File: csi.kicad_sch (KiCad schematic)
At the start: 69 parts, among them J10 Conn_01x22_MountingPin, J11 Conn_01x22_MountingPin, J8 Conn_01x22_MountingPin, J9 Conn_01x22_MountingPin, U16 PI4MSD5V9548AZDEX, U17 AP22615A, U18 AP22615A, U19 AP22615A, U20 AP22615A, U21 NTS0102, U22 NTS0102

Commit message: DRC cleanup
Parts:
- U16: footprint JetsonCarrier:VQFN-24-1EP_3.8x3.8x1.0mm_P0.5mm -> Argus-IC:TQFN-24-1EP_4x4mm_P0.5mm_EP2.3x2.3mm
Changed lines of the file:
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@@
 			)
 		)
-		(property "Footprint" "JetsonCarrier:VQFN-24-1EP_3.8x3.8x1.0mm_P0.5mm"
+		(property "Footprint" "Argus-IC:TQFN-24-1EP_4x4mm_P0.5mm_EP2.3x2.3mm"
 			(at 106.68 66.04 0)
 			(hide yes)

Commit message: Move parts under SoM to bottom for thinner module connector
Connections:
- net VSYNC_CAM0: now also U21.5 (A_{1}); no longer U21.4 (A_{2})
- net VSYNC_CAM0_3V3: now also U21.8 (B_{1}); no longer U21.1 (B_{2})
- net VSYNC_CAM1: now also U21.4 (A_{2}); no longer U21.5 (A_{1})
- net VSYNC_CAM1_3V3: now also U21.1 (B_{2}); no longer U21.8 (B_{1})
- net VSYNC_CAM2: now also U22.5 (A_{1}); no longer U22.4 (A_{2})
- net VSYNC_CAM2_3V3: now also U22.8 (B_{1}); no longer U22.1 (B_{2})
- net VSYNC_CAM3: now also U22.4 (A_{2}); no longer U22.5 (A_{1})
- net VSYNC_CAM3_3V3: now also U22.1 (B_{2}); no longer U22.8 (B_{1})
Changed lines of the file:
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@@
 	)
 	(label "VSYNC_CAM0_3V3"
-		(at 382.27 198.12 180)
+		(at 382.27 195.58 180)
 		(effects
 			(font
@@
 	)
 	(label "VSYNC_CAM1_3V3"
-		(at 382.27 195.58 180)
+		(at 382.27 198.12 180)
 		(effects
 			(font
@@
 	)
 	(label "VSYNC_CAM3_3V3"
-		(at 382.27 227.33 180)
+		(at 382.27 229.87 180)
 		(effects
 			(font
@@
 	)
 	(label "VSYNC_CAM2_3V3"
-		(at 382.27 229.87 180)
+		(at 382.27 227.33 180)
 		(effects
 			(font
@@
 	(global_label "VSYNC_CAM0"
 		(shape input)
-		(at 341.63 198.12 180)
-		(fields_autoplaced yes)
-		(effects
-			(font
-				(size 1.27 1.27)
-			)
-			(justify right)
-		)
-		(property "Intersheetrefs" "${INTERSHEET_REFS}"
-			(at 327.2426 198.1994 0)
+		(at 341.63 195.58 180)
+		(fields_autoplaced yes)
+		(effects
+			(font
+				(size 1.27 1.27)
+			)
+			(justify right)
+		)
+		(property "Intersheetrefs" "${INTERSHEET_REFS}"
+			(at 327.2426 195.5006 0)
 			(show_name no)
 			(do_not_autoplace no)
@@
 	(global_label "VSYNC_CAM2"
 		(shape input)
+		(at 341.63 227.33 180)
+		(fields_autoplaced yes)
+		(effects
+			(font
+				(size 1.27 1.27)
+			)
+			(justify right)
+		)
+		(property "Intersheetrefs" "${INTERSHEET_REFS}"
+			(at 327.2426 227.2506 0)
+			(show_name no)
+			(do_not_autoplace no)
+			(effects
+				(font
+					(size 1.27 1.27)
+				)
+				(justify right)
+			)
+		)
+	)
+	(global_label "CSI2_CLK_P"
+		(shape input)
+		(at 295.91 95.25 180)
+		(fields_autoplaced yes)
+		(effects
+			(font
+				(size 1.27 1.27)
+			)
+			(justify right)
+		)
+		(property "Intersheetrefs" "${INTERSHEET_REFS}"
+			(at 282.4298 95.3294 0)
+			(show_name no)
+			(do_not_autoplace no)
+			(effects
+				(font
+					(size 1.27 1.27)
+				)
+				(justify right)
+			)
+		)
+	)
+	(global_label "VSYNC_CAM3"
+		(shape input)
 		(at 341.63 229.87 180)
 		(fields_autoplaced yes)
@@
 		)
 		(property "Intersheetrefs" "${INTERSHEET_REFS}"
-			(at 327.2426 229.9494 0)
-			(show_name no)
-			(do_not_autoplace no)
-			(effects
-				(font
-					(size 1.27 1.27)
-				)
-				(justify right)
-			)
-		)
-	)
-	(global_label "CSI2_CLK_P"
-		(shape input)
-		(at 295.91 95.25 180)
-		(fields_autoplaced yes)
-		(effects
-			(font
-				(size 1.27 1.27)
-			)
-			(justify right)
-		)
-		(property "Intersheetrefs" "${INTERSHEET_REFS}"
-			(at 282.4298 95.3294 0)
-			(show_name no)
-			(do_not_autoplace no)
-			(effects
-				(font
-					(size 1.27 1.27)
-				)
-				(justify right)
-			)
-		)
-	)
-	(global_label "VSYNC_CAM3"
-		(shape input)
-		(at 341.63 227.33 180)
-		(fields_autoplaced yes)
-		(effects
-			(font
-				(size 1.27 1.27)
-			)
-			(justify right)
-		)
-		(property "Intersheetrefs" "${INTERSHEET_REFS}"
-			(at 327.2426 227.4094 0)
+			(at 327.2426 229.7906 0)
 			(show_name no)
 			(do_not_autoplace no)
@@
 	(global_label "VSYNC_CAM1"
 		(shape input)
-		(at 341.63 195.58 180)
-		(fields_autoplaced yes)
-		(effects
-			(font
-				(size 1.27 1.27)
-			)
-			(justify right)
-		)
-		(property "Intersheetrefs" "${INTERSHEET_REFS}"
-			(at 327.2426 195.6594 0)
-			(show_name no)
-			(do_not_autoplace no)
+		(at 341.63 198.12 180)
+		(fields_autoplaced yes)
+		(effects
+			(font
+				(size 1.27 1.27)
+			)
+			(justify right)
+		)
+		(property "Intersheetrefs" "${INTERSHEET_REFS}"
+			(at 327.2426 198.0406 0)
+			(show_name no)
+			(do_not_autoplace no)

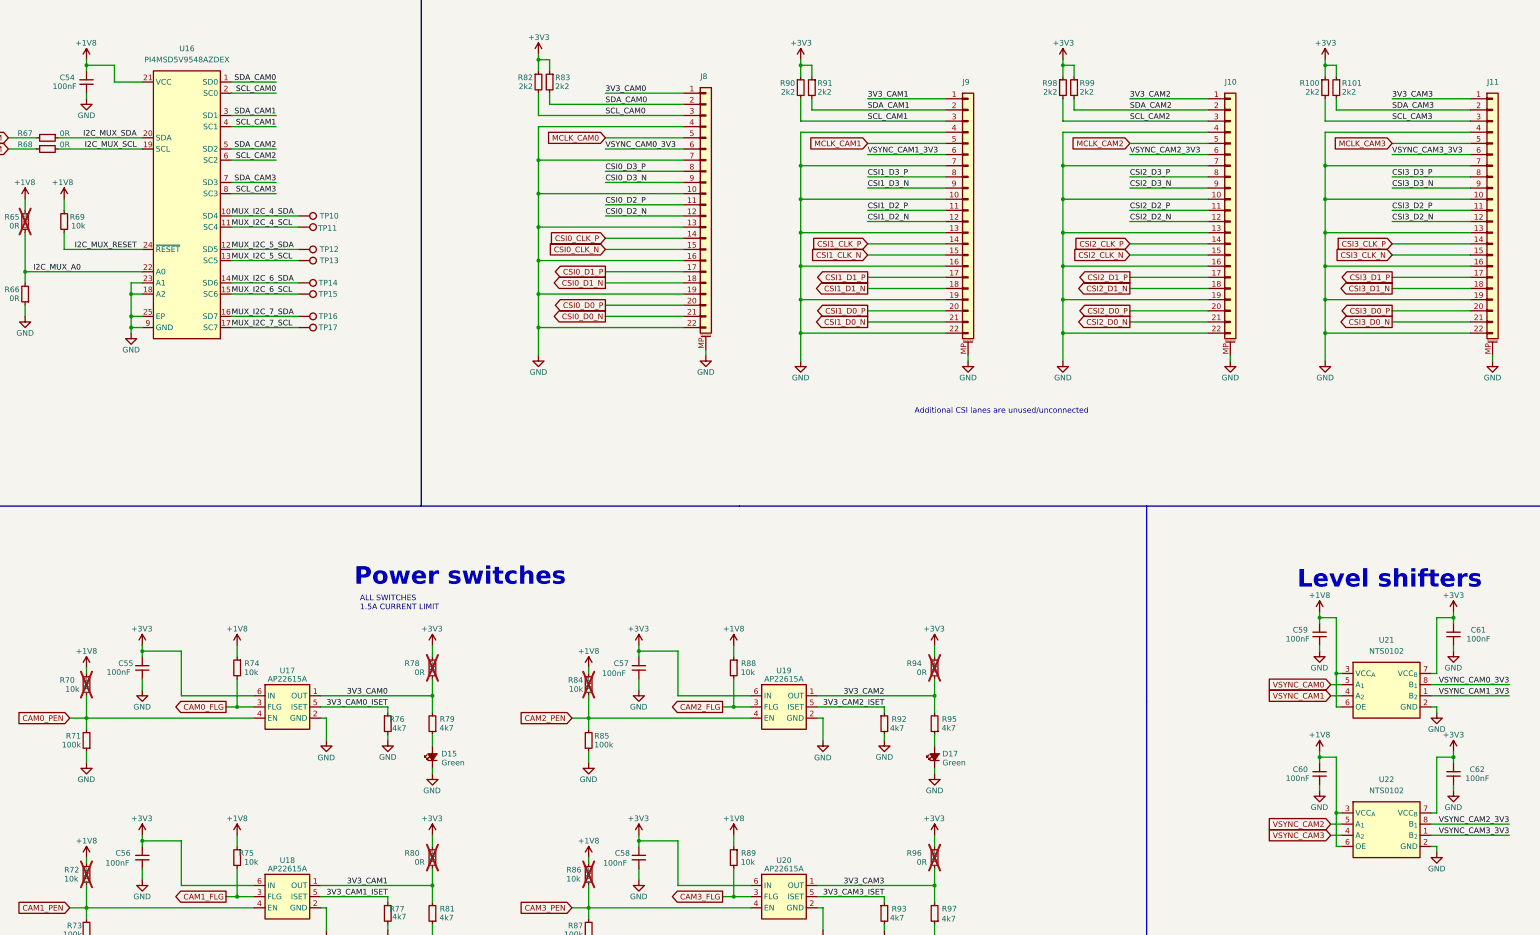
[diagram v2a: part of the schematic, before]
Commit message: Replace current monitor w/ INA226 (addr = 0x42)
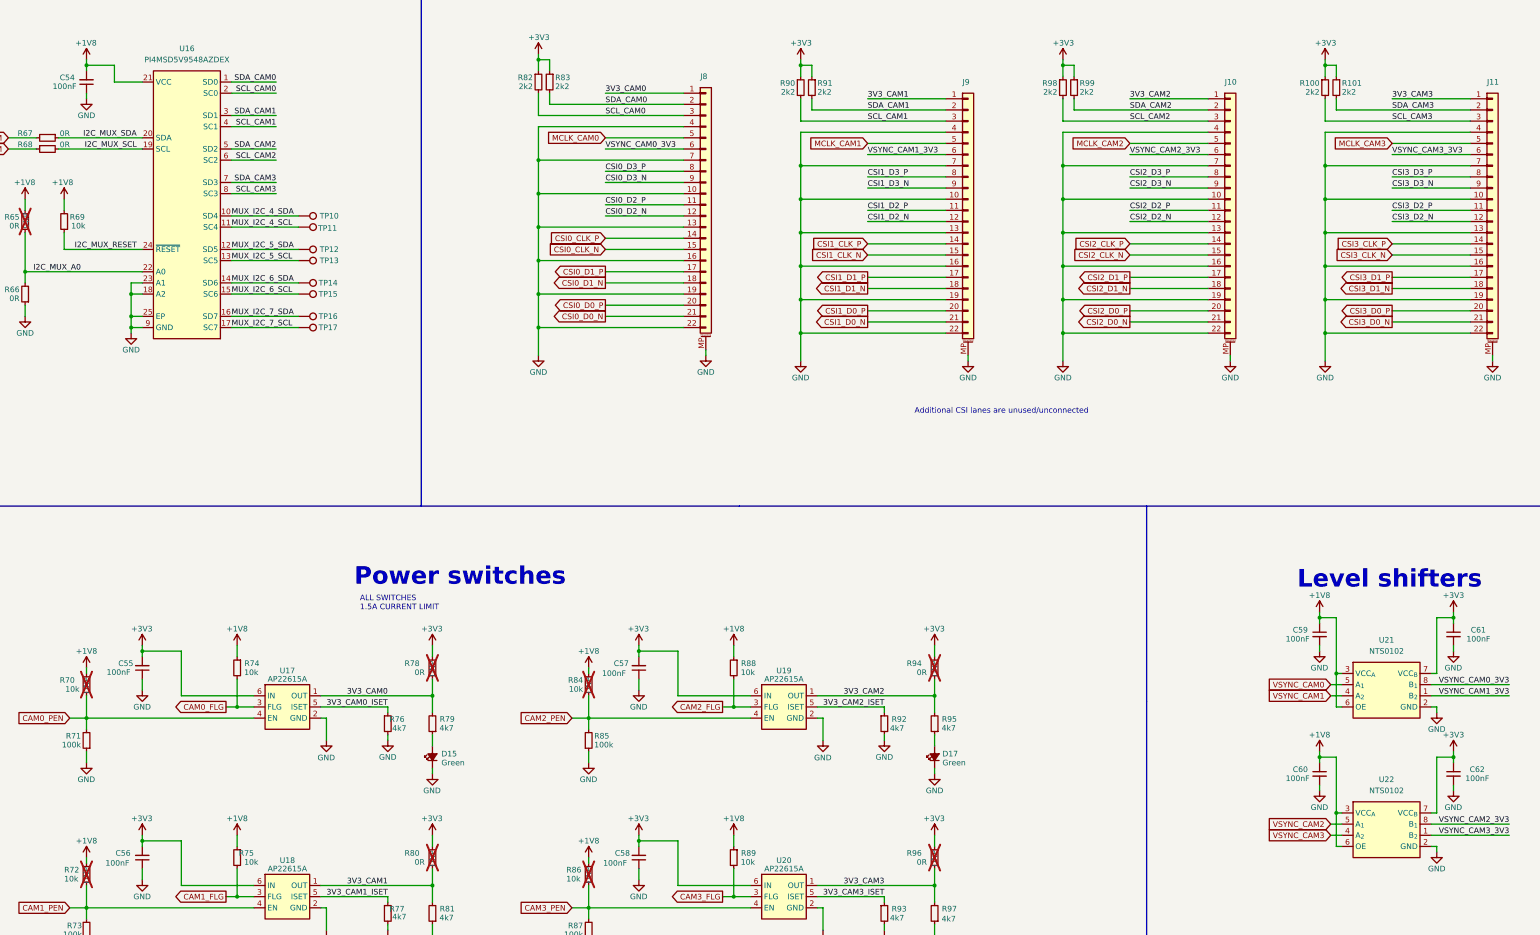
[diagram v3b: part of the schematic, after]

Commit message: Final BOM changes, gerbers
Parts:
- C54, C55, C56, C57, C58, C59, C60, C61, C62: LCSC (none) -> C14663
- D15, D16, D17, D18: LCSC (none) -> C12065
- R100, R101, R82, R83, R90, R91, R98, R99: LCSC (none) -> C4190
- R65, R66, R67, R68: LCSC (none) -> C17168
- R69, R70, R72, R74, R75, R84, R86, R88, R89: LCSC (none) -> C25804
- R71, R73, R85, R87: LCSC (none) -> C25803
- R76, R77, R79, R81, R92, R93, R95, R97: LCSC (none) -> C23162
- R78, R80, R94, R96: LCSC (none) -> C21189
- U16: LCSC (none) -> C2674581
- U17, U18, U19, U20: LCSC (none) -> C2680357
- U21, U22: LCSC (none) -> C2687851
